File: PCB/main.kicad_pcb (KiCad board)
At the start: 2 copper layers, 53.1 x 58.4 mm, 39 parts, among them CON1 BARREL_JACK, P1 JUMPER_LEFT, P2 LEFT, P3 JUMPER_RIGHT, P4 RIGHT, Q1 3904, Q2 3904, Q3 3904, Q4 3904, SW1 12x12_PUSHBUTTON_SPST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

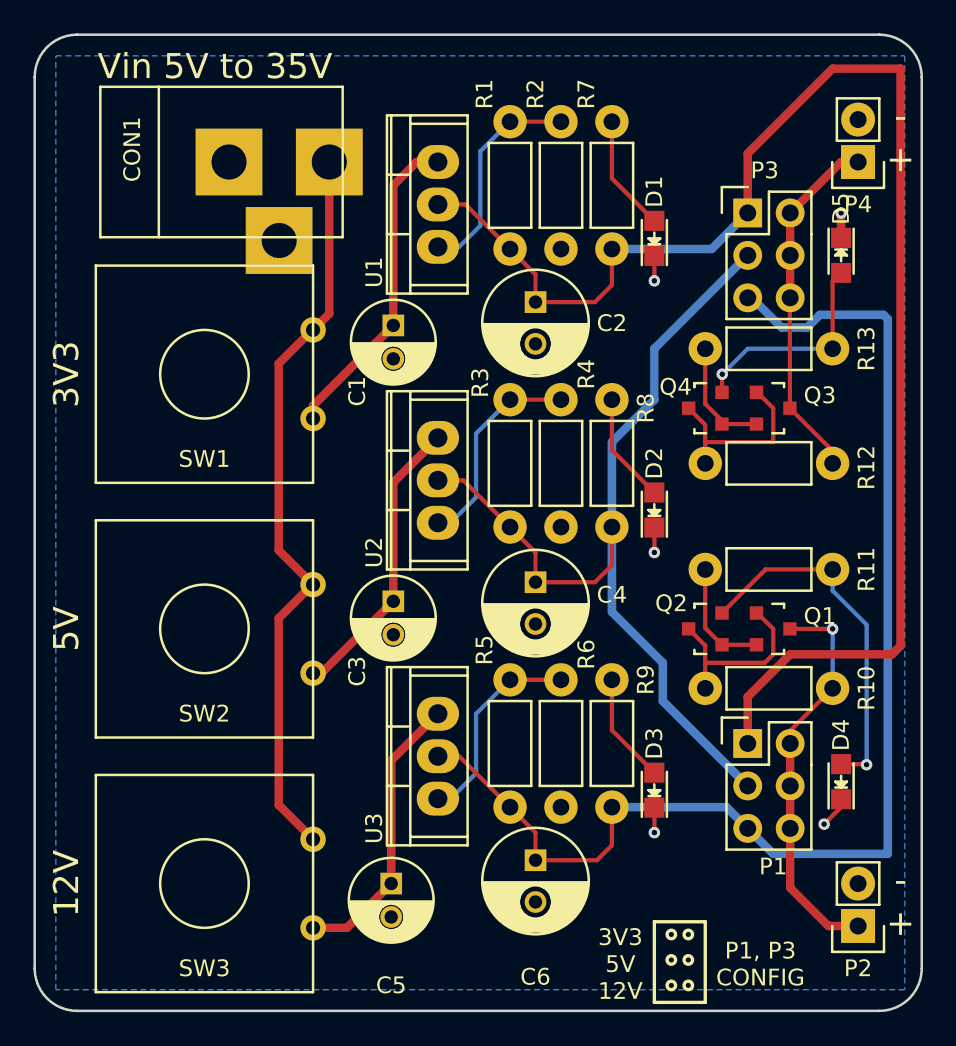
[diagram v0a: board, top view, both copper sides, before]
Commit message: Some pads hole size modification.
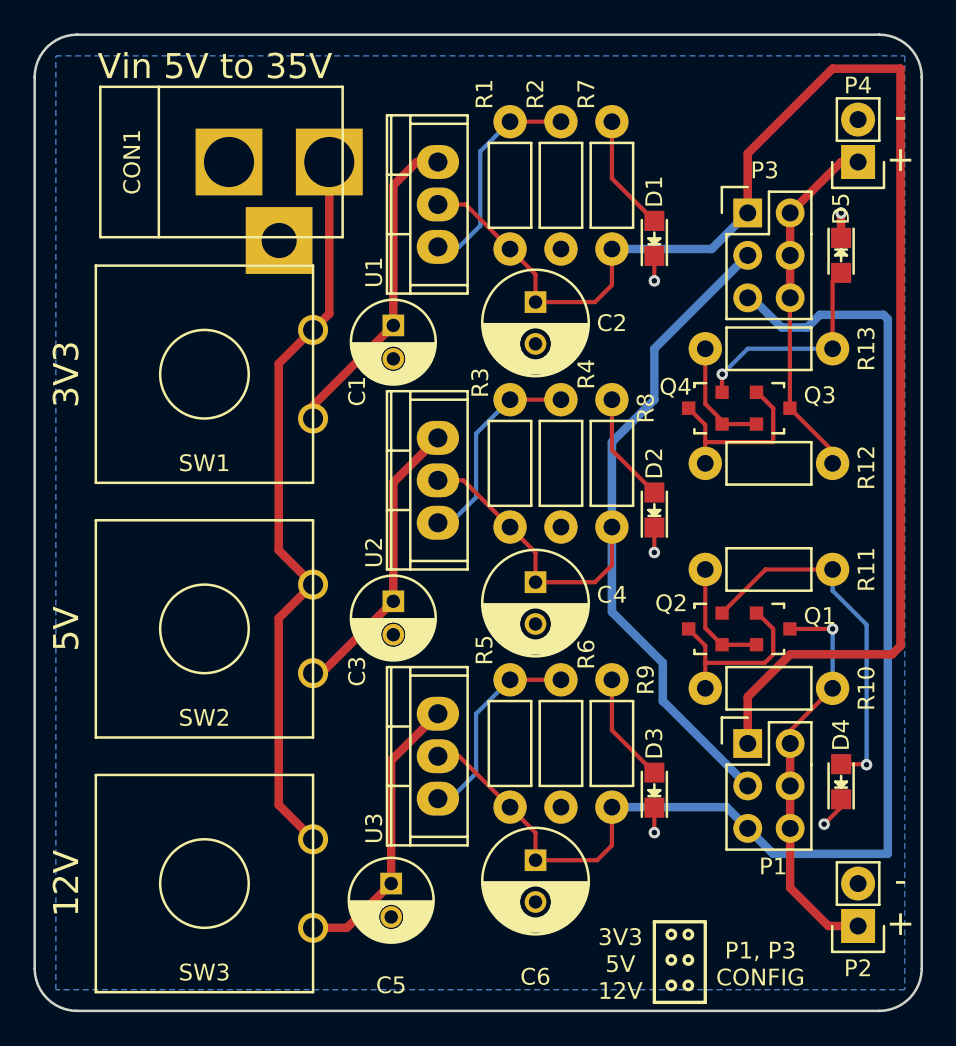
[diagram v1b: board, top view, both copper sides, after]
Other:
- board text added: "Breadboard Power Supply v0.2 By : Yannick Gagne"
- board text removed: "Breadboard Power Supply v0.1 By : Yannick Gagne"
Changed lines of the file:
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@@
     (add_net "Net-(R5-Pad2)")
-  )
-  (module mods:BARREL_JACK2 (layer F.Cu)
-    (at 64.77 27.94)
-    (descr "DC Barrel Jack")
-    (tags "Power Jack")
-    (fp_text reference CON1 (at -5.588 -0.762 90) (layer F.SilkS)
-      (effects (font (size 1 1) (thickness 0.15)))
-    )
-    (fp_text value BARREL_JACK (at 0 -5.99948) (layer F.Fab)
-      (effects (font (size 1 1) (thickness 0.15)))
-    )
-    (fp_line (start -4.0005 -4.50088) (end -4.0005 4.50088) (layer F.SilkS) (width 0.15))
-    (fp_line (start -7.50062 -4.50088) (end -7.50062 4.50088) (layer F.SilkS) (width 0.15))
-    (fp_line (start -7.50062 4.50088) (end 7.00024 4.50088) (layer F.SilkS) (width 0.15))
-    (fp_line (start 7.00024 4.50088) (end 7.00024 -4.50088) (layer F.SilkS) (width 0.15))
-    (fp_line (start 7.00024 -4.50088) (end -7.50062 -4.50088) (layer F.SilkS) (width 0.15))
-    (pad 1 thru_hole rect (at 6.20014 0) (size 4 4) (drill 2.1) (layers *.Cu *.Mask F.SilkS)
-      (net 8 "Net-(CON1-Pad1)"))
-    (pad 2 thru_hole rect (at 0.20066 0) (size 4 4) (drill 2.1) (layers *.Cu *.Mask F.SilkS)
-      (net 2 GND))
-    (pad 3 thru_hole rect (at 3.2004 4.699) (size 4 4) (drill 2.1) (layers *.Cu *.Mask F.SilkS)
-      (net 9 "Net-(CON1-Pad3)"))
   )
   (module Resistors_ThroughHole:Resistor_Horizontal_RM7mm (layer F.Cu)
@@
     (descr "Through hole pin header")
     (tags "pin header")
-    (fp_text reference P4 (at 0 -2.54 180) (layer F.SilkS)
+    (fp_text reference P4 (at 0 4.572 180) (layer F.SilkS)
       (effects (font (size 1 1) (thickness 0.15)))
     )
@@
     (pad 1 thru_hole oval (at -2.54 0 90) (size 2.032 2.54) (drill 1.143) (layers *.Cu *.Mask F.SilkS)
       (net 23 "Net-(R5-Pad2)"))
-  )
-  (module myparts:12x12_PUSHBUTTON_SPST (layer F.Cu)
-    (at 63.5 40.64)
-    (fp_text reference SW1 (at 0 5.08) (layer F.SilkS)
-      (effects (font (size 1 1) (thickness 0.15)))
-    )
-    (fp_text value 12x12_PUSHBUTTON_SPST (at -7.62 -3.81 90) (layer F.Fab) hide
-      (effects (font (size 1 1) (thickness 0.15)))
-    )
-    (fp_circle (center 0 0) (end 2.65 0) (layer F.SilkS) (width 0.15))
-    (fp_line (start -6.5 -6.5) (end 6.5 -6.5) (layer F.SilkS) (width 0.15))
-    (fp_line (start 6.5 -6.5) (end 6.5 6.5) (layer F.SilkS) (width 0.15))
-    (fp_line (start 6.5 6.5) (end -6.5 6.5) (layer F.SilkS) (width 0.15))
-    (fp_line (start -6.5 6.5) (end -6.5 -6.5) (layer F.SilkS) (width 0.15))
-    (pad 1 thru_hole circle (at 6.5 -2.65) (size 1.524 1.524) (drill 0.85) (layers *.Cu *.Mask F.SilkS)
-      (net 8 "Net-(CON1-Pad1)"))
-    (pad 2 thru_hole circle (at 6.5 2.65) (size 1.524 1.524) (drill 0.85) (layers *.Cu *.Mask F.SilkS)
-      (net 1 "Net-(C1-Pad1)"))
-  )
-  (module myparts:12x12_PUSHBUTTON_SPST (layer F.Cu)
-    (at 63.5 55.88)
-    (fp_text reference SW2 (at 0 5.08) (layer F.SilkS)
-      (effects (font (size 1 1) (thickness 0.15)))
-    )
-    (fp_text value 12x12_PUSHBUTTON_SPST (at -7.62 -3.81 90) (layer F.Fab) hide
-      (effects (font (size 1 1) (thickness 0.15)))
-    )
-    (fp_circle (center 0 0) (end 2.65 0) (layer F.SilkS) (width 0.15))
-    (fp_line (start -6.5 -6.5) (end 6.5 -6.5) (layer F.SilkS) (width 0.15))
-    (fp_line (start 6.5 -6.5) (end 6.5 6.5) (layer F.SilkS) (width 0.15))
-    (fp_line (start 6.5 6.5) (end -6.5 6.5) (layer F.SilkS) (width 0.15))
-    (fp_line (start -6.5 6.5) (end -6.5 -6.5) (layer F.SilkS) (width 0.15))
-    (pad 1 thru_hole circle (at 6.5 -2.65) (size 1.524 1.524) (drill 0.85) (layers *.Cu *.Mask F.SilkS)
-      (net 8 "Net-(CON1-Pad1)"))
-    (pad 2 thru_hole circle (at 6.5 2.65) (size 1.524 1.524) (drill 0.85) (layers *.Cu *.Mask F.SilkS)
-      (net 4 "Net-(C3-Pad1)"))
-  )
-  (module myparts:12x12_PUSHBUTTON_SPST (layer F.Cu)
-    (at 63.5 71.12)
-    (fp_text reference SW3 (at 0 5.08) (layer F.SilkS)
-      (effects (font (size 1 1) (thickness 0.15)))
-    )
-    (fp_text value 12x12_PUSHBUTTON_SPST (at -7.62 -3.81 90) (layer F.Fab) hide
-      (effects (font (size 1 1) (thickness 0.15)))
-    )
-    (fp_circle (center 0 0) (end 2.65 0) (layer F.SilkS) (width 0.15))
-    (fp_line (start -6.5 -6.5) (end 6.5 -6.5) (layer F.SilkS) (width 0.15))
-    (fp_line (start 6.5 -6.5) (end 6.5 6.5) (layer F.SilkS) (width 0.15))
-    (fp_line (start 6.5 6.5) (end -6.5 6.5) (layer F.SilkS) (width 0.15))
-    (fp_line (start -6.5 6.5) (end -6.5 -6.5) (layer F.SilkS) (width 0.15))
-    (pad 1 thru_hole circle (at 6.5 -2.65) (size 1.524 1.524) (drill 0.85) (layers *.Cu *.Mask F.SilkS)
-      (net 8 "Net-(CON1-Pad1)"))
-    (pad 2 thru_hole circle (at 6.5 2.65) (size 1.524 1.524) (drill 0.85) (layers *.Cu *.Mask F.SilkS)
-      (net 6 "Net-(C5-Pad1)"))
   )
   (module Capacitors_ThroughHole:C_Radial_D6.3_L11.2_P2.5 (layer F.Cu)
@@
     )
   )
+  (module mods:BARREL_JACK2 (layer F.Cu)
+    (at 64.77 27.94)
+    (descr "DC Barrel Jack")
+    (tags "Power Jack")
+    (fp_text reference CON1 (at -5.588 0 90) (layer F.SilkS)
+      (effects (font (size 1 1) (thickness 0.15)))
+    )
+    (fp_text value BARREL_JACK (at 0 -5.99948) (layer F.Fab) hide
+      (effects (font (size 1 1) (thickness 0.15)))
+    )
+    (fp_line (start -4.0005 -4.50088) (end -4.0005 4.50088) (layer F.SilkS) (width 0.15))
+    (fp_line (start -7.50062 -4.50088) (end -7.50062 4.50088) (layer F.SilkS) (width 0.15))
+    (fp_line (start -7.50062 4.50088) (end 7.00024 4.50088) (layer F.SilkS) (width 0.15))
+    (fp_line (start 7.00024 4.50088) (end 7.00024 -4.50088) (layer F.SilkS) (width 0.15))
+    (fp_line (start 7.00024 -4.50088) (end -7.50062 -4.50088) (layer F.SilkS) (width 0.15))
+    (pad 1 thru_hole rect (at 6.20014 0) (size 4 4) (drill 3) (layers *.Cu *.Mask F.SilkS)
+      (net 8 "Net-(CON1-Pad1)"))
+    (pad 2 thru_hole rect (at 0.20066 0) (size 4 4) (drill 3) (layers *.Cu *.Mask F.SilkS)
+      (net 2 GND))
+    (pad 3 thru_hole rect (at 3.2004 4.699) (size 4 4) (drill 2.1) (layers *.Cu *.Mask F.SilkS)
+      (net 9 "Net-(CON1-Pad3)"))
+  )
+  (module myparts:12x12_PUSHBUTTON_SPST (layer F.Cu)
+    (at 63.5 40.64)
+    (fp_text reference SW1 (at 0 5.334) (layer F.SilkS)
+      (effects (font (size 1 1) (thickness 0.15)))
+    )
+    (fp_text value 12x12_PUSHBUTTON_SPST (at 0 -7.366) (layer F.Fab) hide
+      (effects (font (size 1 1) (thickness 0.15)))
+    )
+    (fp_circle (center 0 0) (end 2.65 0) (layer F.SilkS) (width 0.15))
+    (fp_line (start -6.5 -6.5) (end 6.5 -6.5) (layer F.SilkS) (width 0.15))
+    (fp_line (start 6.5 -6.5) (end 6.5 6.5) (layer F.SilkS) (width 0.15))
+    (fp_line (start 6.5 6.5) (end -6.5 6.5) (layer F.SilkS) (width 0.15))
+    (fp_line (start -6.5 6.5) (end -6.5 -6.5) (layer F.SilkS) (width 0.15))
+    (pad 1 thru_hole circle (at 6.5 -2.65) (size 1.8 1.8) (drill 1.2) (layers *.Cu *.Mask F.SilkS)
+      (net 8 "Net-(CON1-Pad1)"))
+    (pad 2 thru_hole circle (at 6.5 2.65) (size 1.8 1.8) (drill 1.2) (layers *.Cu *.Mask F.SilkS)
+      (net 1 "Net-(C1-Pad1)"))
+  )
+  (module myparts:12x12_PUSHBUTTON_SPST (layer F.Cu)
+    (at 63.5 55.88)
+    (fp_text reference SW2 (at 0 5.334) (layer F.SilkS)
+      (effects (font (size 1 1) (thickness 0.15)))
+    )
+    (fp_text value 12x12_PUSHBUTTON_SPST (at 0 -7.366) (layer F.Fab) hide
+      (effects (font (size 1 1) (thickness 0.15)))
+    )
+    (fp_circle (center 0 0) (end 2.65 0) (layer F.SilkS) (width 0.15))
+    (fp_line (start -6.5 -6.5) (end 6.5 -6.5) (layer F.SilkS) (width 0.15))
+    (fp_line (start 6.5 -6.5) (end 6.5 6.5) (layer F.SilkS) (width 0.15))
+    (fp_line (start 6.5 6.5) (end -6.5 6.5) (layer F.SilkS) (width 0.15))
+    (fp_line (start -6.5 6.5) (end -6.5 -6.5) (layer F.SilkS) (width 0.15))
+    (pad 1 thru_hole circle (at 6.5 -2.65) (size 1.8 1.8) (drill 1.2) (layers *.Cu *.Mask F.SilkS)
+      (net 8 "Net-(CON1-Pad1)"))
+    (pad 2 thru_hole circle (at 6.5 2.65) (size 1.8 1.8) (drill 1.2) (layers *.Cu *.Mask F.SilkS)
+      (net 4 "Net-(C3-Pad1)"))
+  )
+  (module myparts:12x12_PUSHBUTTON_SPST (layer F.Cu)
+    (at 63.5 71.12)
+    (fp_text reference SW3 (at 0 5.334) (layer F.SilkS)
+      (effects (font (size 1 1) (thickness 0.15)))
+    )
+    (fp_text value 12x12_PUSHBUTTON_SPST (at 0 -7.366) (layer F.Fab) hide
+      (effects (font (size 1 1) (thickness 0.15)))
+    )
+    (fp_circle (center 0 0) (end 2.65 0) (layer F.SilkS) (width 0.15))
+    (fp_line (start -6.5 -6.5) (end 6.5 -6.5) (layer F.SilkS) (width 0.15))
+    (fp_line (start 6.5 -6.5) (end 6.5 6.5) (layer F.SilkS) (width 0.15))
+    (fp_line (start 6.5 6.5) (end -6.5 6.5) (layer F.SilkS) (width 0.15))
+    (fp_line (start -6.5 6.5) (end -6.5 -6.5) (layer F.SilkS) (width 0.15))
+    (pad 1 thru_hole circle (at 6.5 -2.65) (size 1.8 1.8) (drill 1.2) (layers *.Cu *.Mask F.SilkS)
+      (net 8 "Net-(CON1-Pad1)"))
+    (pad 2 thru_hole circle (at 6.5 2.65) (size 1.8 1.8) (drill 1.2) (layers *.Cu *.Mask F.SilkS)
+      (net 6 "Net-(C5-Pad1)"))
+  )
   (gr_text "Vin 5V to 35V" (at 64.135 22.225) (layer F.SilkS)
     (effects (font (size 1.5 1.5) (thickness 0.3)))
@@
     (effects (font (size 1 1) (thickness 0.2)))
   )
-  (gr_text "Breadboard Power Supply v0.1\nBy : Yannick Gagne" (at 60.452 54.864 90) (layer B.SilkS)
+  (gr_text "Breadboard Power Supply v0.2\nBy : Yannick Gagne" (at 60.452 54.864 90) (layer B.SilkS)
     (effects (font (size 1.5 1.5) (thickness 0.3)) (justify mirror))
   )

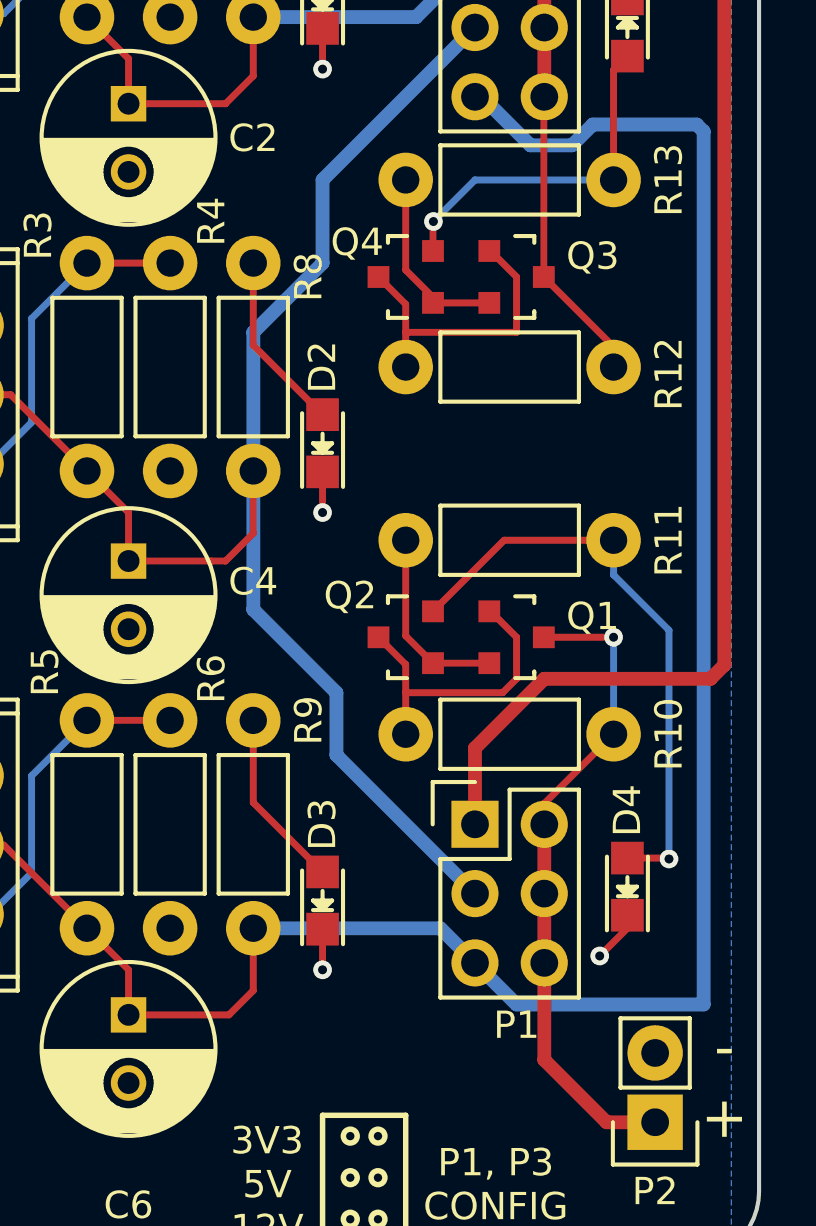
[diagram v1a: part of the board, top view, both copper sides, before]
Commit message: added jumper for disconnected ground plane section
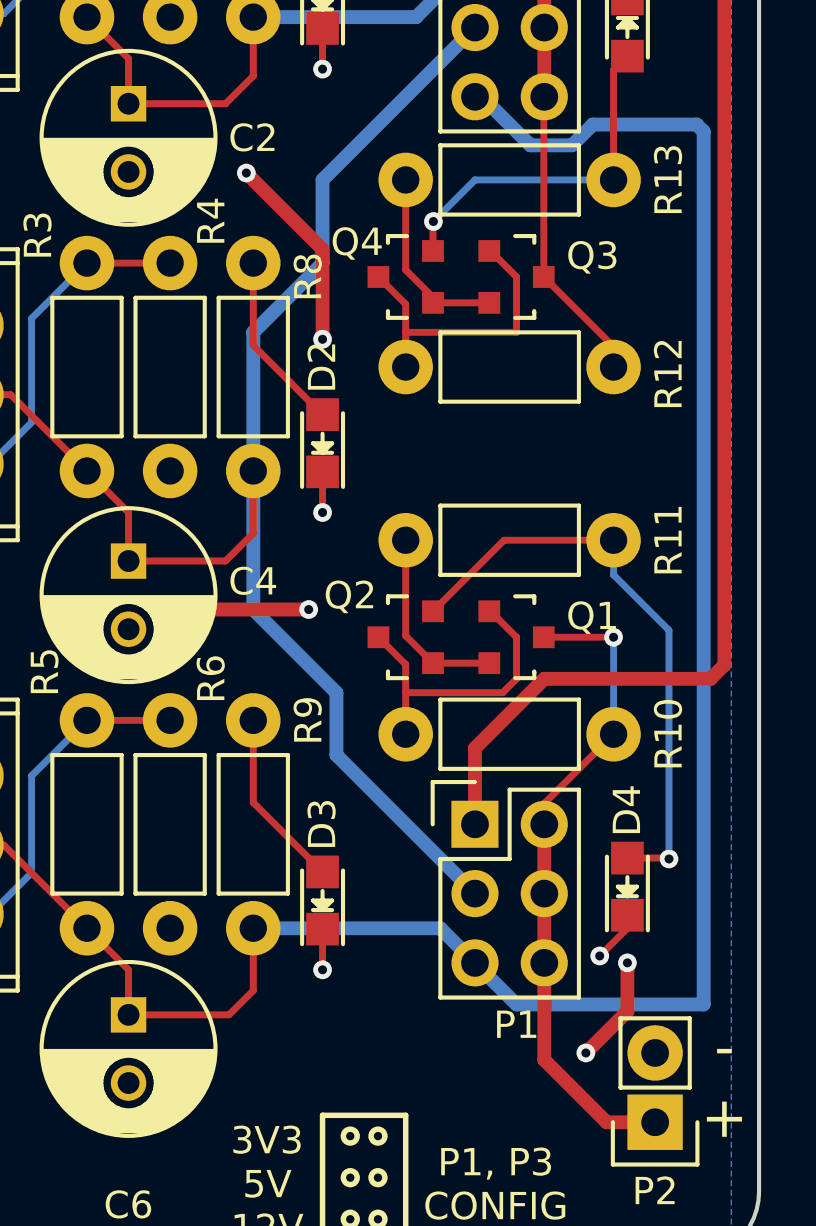
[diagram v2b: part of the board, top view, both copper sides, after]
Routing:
- net GND: track 7.88 -> 23.4 mm, vias 5 -> 11
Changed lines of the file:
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@@
   (general
     (links 71)
-    (no_connects 1)
+    (no_connects 0)
     (area 53.264999 20.244999 106.501001 78.815001)
     (thickness 1.524)
     (drawings 27)
-    (tracks 161)
+    (tracks 172)
     (zones 0)
     (modules 39)
@@
   )
   (setup
-    (last_trace_width 0.1524)
+    (last_trace_width 0.508)
     (user_trace_width 0.254)
     (user_trace_width 0.508)
@@
   (segment (start 70 43.29) (end 70 42.522) (width 0.508) (layer F.Cu) (net 1))
   (segment (start 70 42.522) (end 74.803 37.719) (width 0.508) (layer F.Cu) (net 1))
+  (via (at 87.63 38.862) (size 0.6858) (drill 0.3302) (layers F.Cu B.Cu) (net 2))
+  (via (at 90.424 44.958) (size 0.6858) (drill 0.3302) (layers F.Cu B.Cu) (net 2))
+  (segment (start 90.424 44.958) (end 90.424 41.656) (width 0.508) (layer F.Cu) (net 2))
+  (segment (start 90.424 41.656) (end 87.63 38.862) (width 0.508) (layer F.Cu) (net 2))
+  (via (at 100.076 71.12) (size 0.6858) (drill 0.3302) (layers F.Cu B.Cu) (net 2))
+  (via (at 101.6 67.818) (size 0.6858) (drill 0.3302) (layers F.Cu B.Cu) (net 2))
+  (segment (start 101.6 67.818) (end 101.6 69.596) (width 0.508) (layer F.Cu) (net 2))
+  (segment (start 101.6 69.596) (end 100.076 71.12) (width 0.508) (layer F.Cu) (net 2))
+  (via (at 85.598 54.864) (size 0.6858) (drill 0.3302) (layers F.Cu B.Cu) (net 2))
+  (via (at 89.916 54.864) (size 0.6858) (drill 0.3302) (layers F.Cu B.Cu) (net 2))
+  (segment (start 85.598 54.864) (end 89.916 54.864) (width 0.508) (layer F.Cu) (net 2))
   (segment (start 101.6 32.47898) (end 101.6 30.988) (width 0.508) (layer F.Cu) (net 2))
   (via (at 101.6 30.988) (size 0.6858) (drill 0.3302) (layers F.Cu B.Cu) (net 2))

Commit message: Confirmed all v0.2 mods
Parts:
- C1, C3, C5: value 0.1uF -> (none)
- C2, C4, C6: value 220uF -> (none)
- D3: value LED -> (none)
- D4: value Led_Small -> (none)
- P1: value JUMPER_LEFT -> (none)
- P2: value LEFT -> (none)
- R10, R12: value 10k -> (none)
- R13: value 680 -> (none)
- R3: value 150 -> (none)
- R4: value 470 -> (none)
- R5: value 330 -> (none)
- R6: value 2870 -> (none)
- R8: value 180 -> (none)
- R9: value 560 -> (none)
- SW1, SW2, SW3: value 12x12_PUSHBUTTON_SPST -> (none)
- U1, U2, U3: value LM317T -> (none)
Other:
- net class Default: clearance 0.1524 -> 0.006; trace_width 0.1524 -> 0.006; via_dia 0.6858 -> 0.027; via_drill 0.3302 -> 0.013
- rule pad_to_mask_clearance: 0.2 -> 0.0508
- rule trace_clearance: 0.1524 -> 0.006
- rule trace_min: 0.1524 -> 0.006
- rule via_min_drill: 0.3302 -> 0.01
- rule via_min_size: 0.6858 -> 0.02
